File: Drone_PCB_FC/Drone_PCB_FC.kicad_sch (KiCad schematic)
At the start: 0 parts

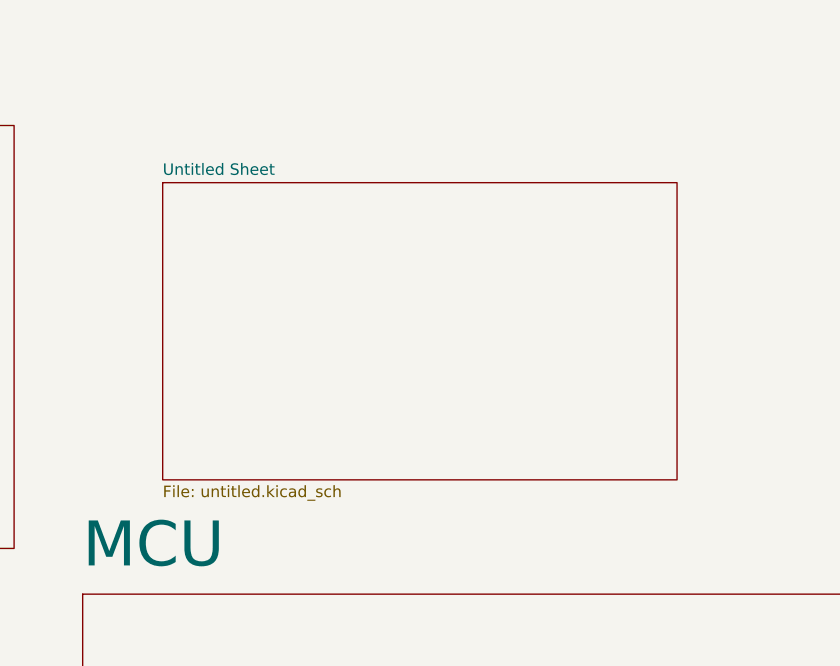
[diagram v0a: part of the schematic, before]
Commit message: almost done with the schmatic design
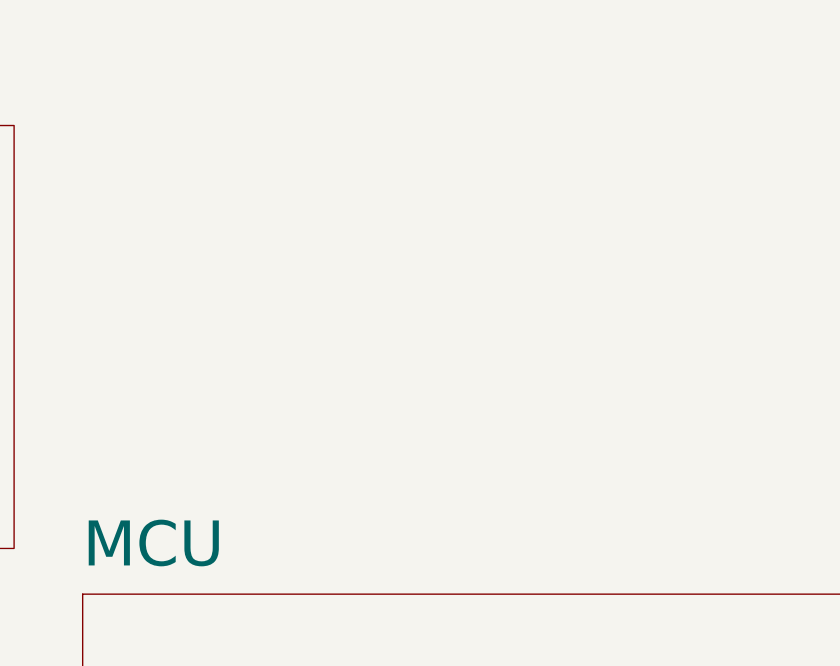
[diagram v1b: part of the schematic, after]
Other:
- removed sheet Untitled Sheet
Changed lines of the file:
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@@
-		)
-	)
-	(sheet
-		(at 105.41 33.02)
-		(size 57.15 33.02)
-		(exclude_from_sim no)
-		(in_bom yes)
-		(on_board yes)
-		(dnp no)
-		(fields_autoplaced yes)
-		(stroke
-			(width 0.1524)
-			(type solid)
-		)
-		(fill
-			(color 0 0 0 0)
-		)
-		(property "Sheetname" "Untitled Sheet"
-			(at 105.41 32.3084 0)
-			(show_name no)
-			(do_not_autoplace no)
-			(effects
-				(font
-					(size 1.27 1.27)
-				)
-				(justify left bottom)
-			)
-		)
-		(property "Sheetfile" "untitled.kicad_sch"
-			(at 105.41 66.6246 0)
-			(show_name no)
-			(do_not_autoplace no)
-			(effects
-				(font
-					(size 1.27 1.27)
-				)
-				(justify left top)
-			)
-		)
-		(instances
-			(project "Drone_PCB_FC"
-				(path "/30482008-3d6c-427d-9917-9811da561e6b"
-					(page "9")
-				)
-			)
 		)
 	)
